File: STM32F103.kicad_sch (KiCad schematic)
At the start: 8 parts, among them SW1 SW_MEC_5E, U1 STM32F103CBTx

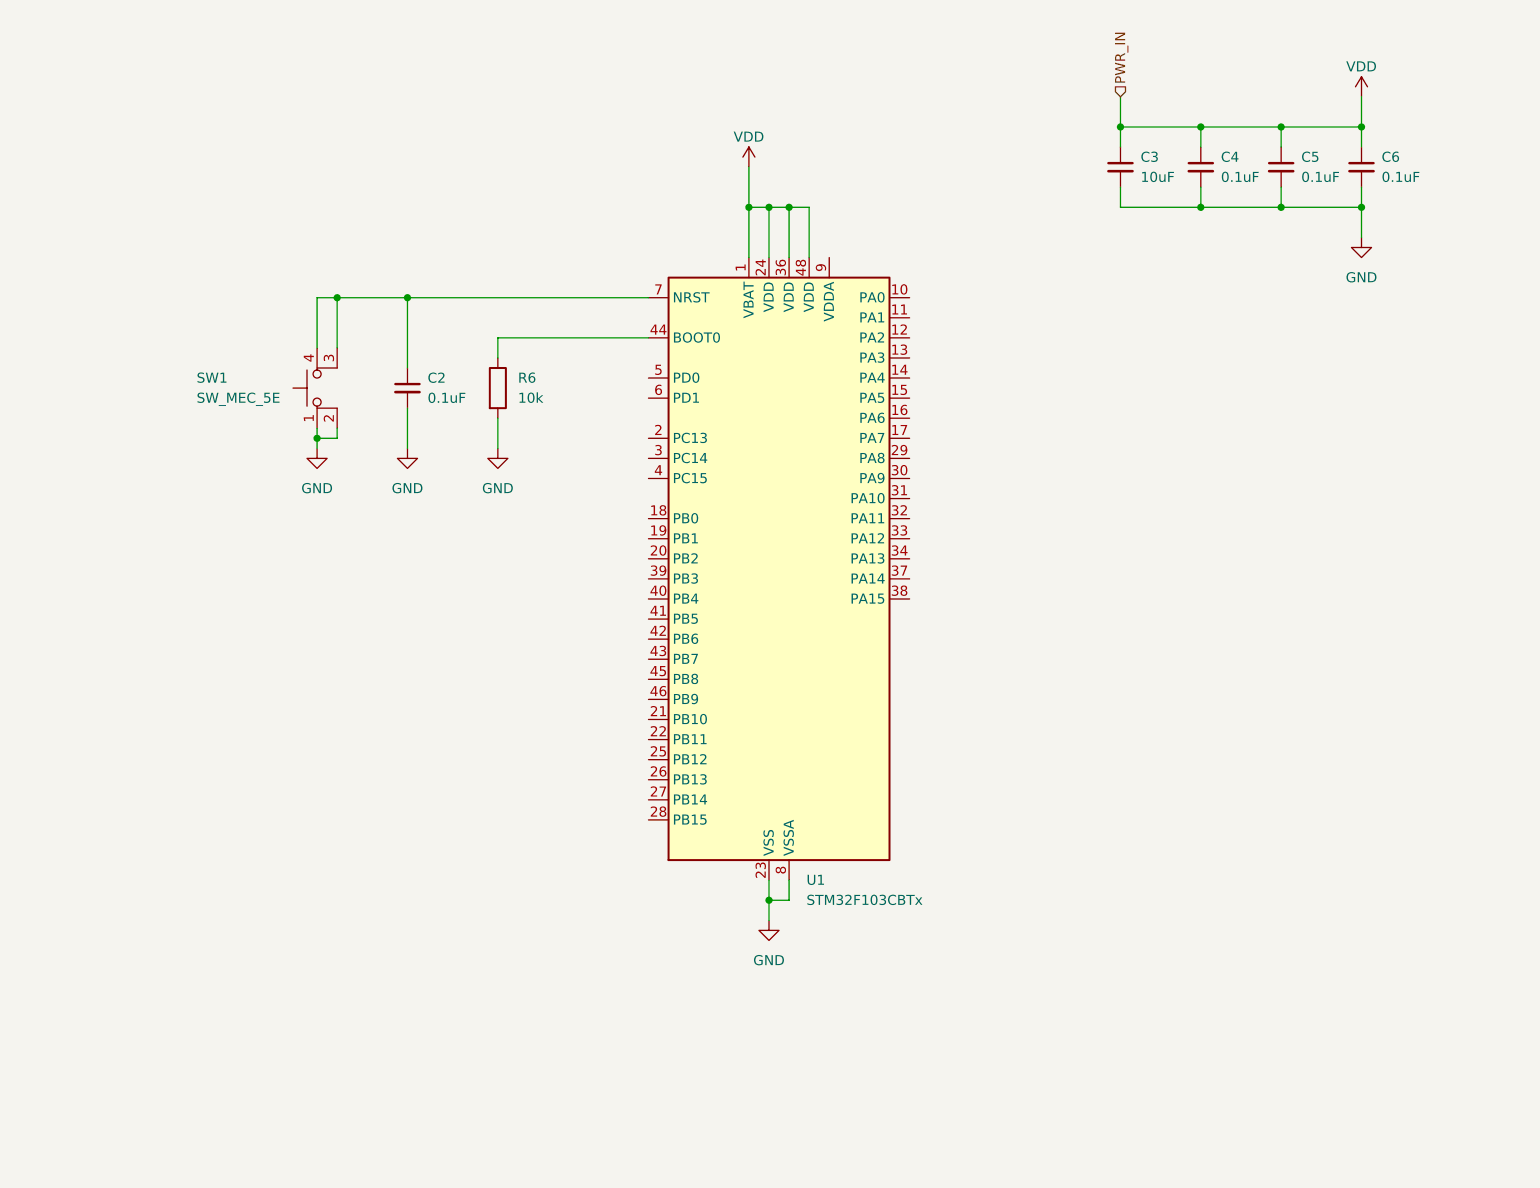
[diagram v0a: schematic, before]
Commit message: add STM32F103
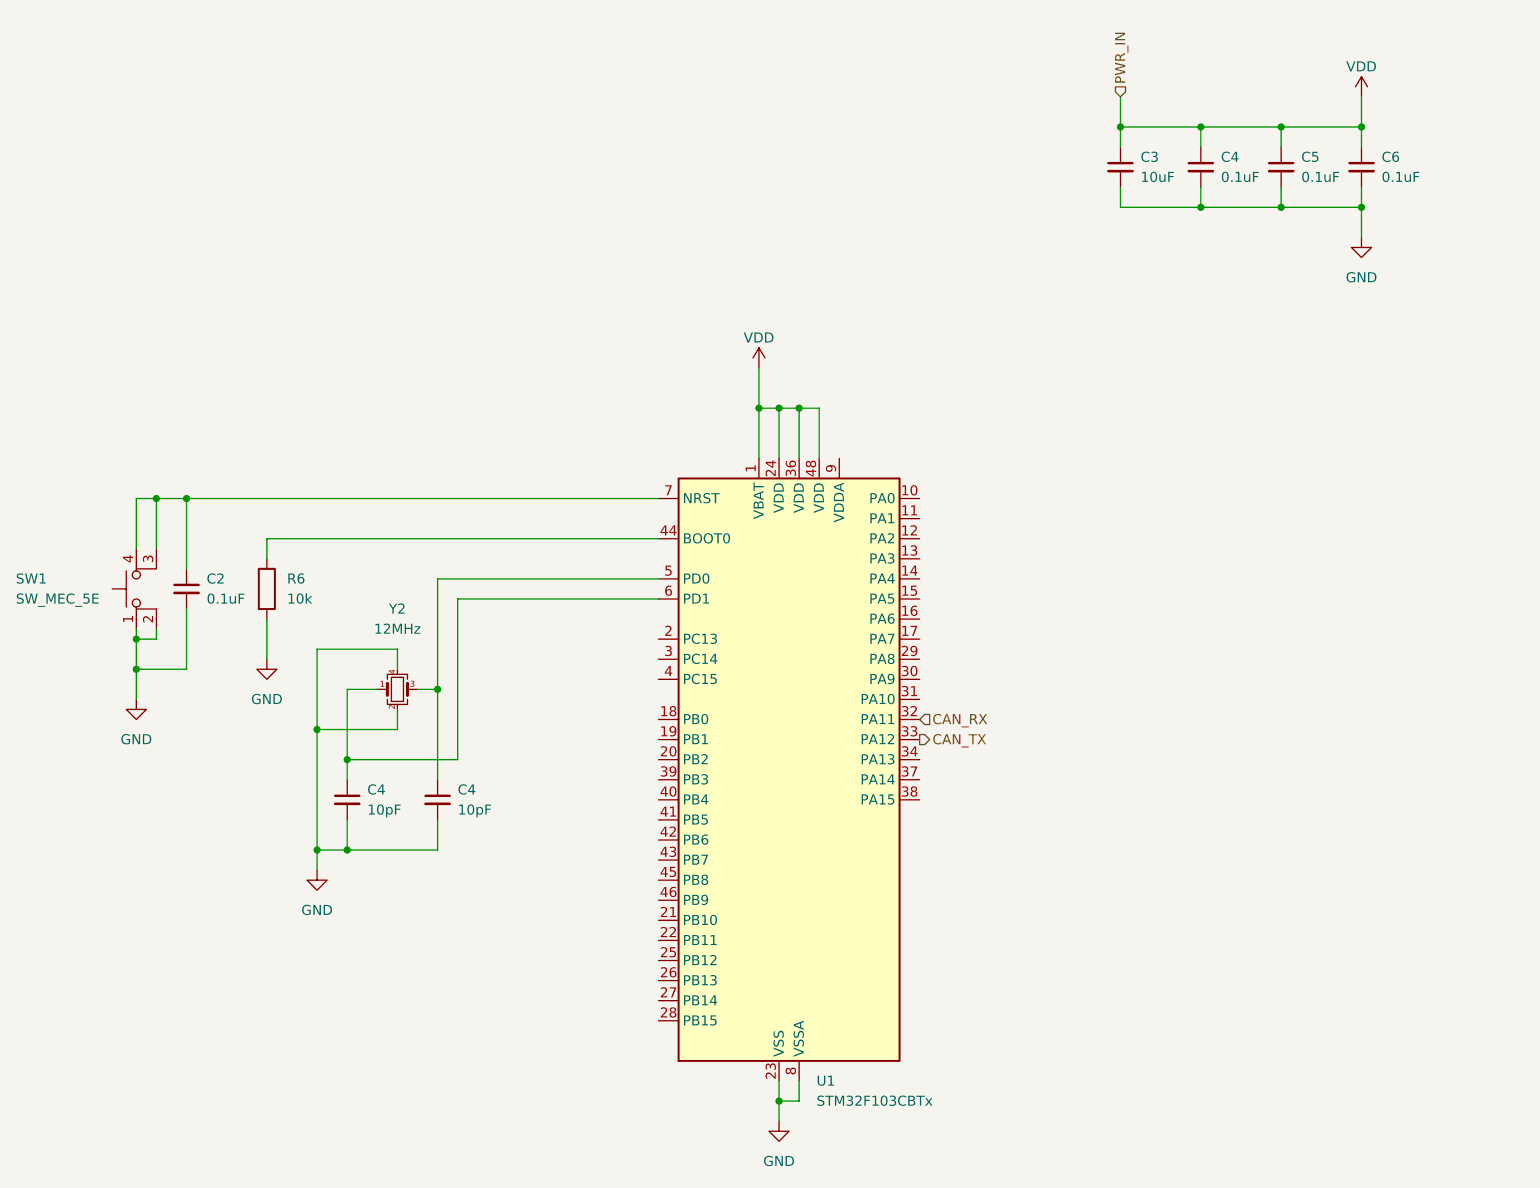
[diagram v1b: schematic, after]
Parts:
- added C4 (x2): 10pF, Capacitor_SMD:C_0603_1608Metric_Pad1.08x0.95mm_HandSolder, symbol Device:C_Small
- added Y2: 12MHz, symbol Device:Crystal_GND24_Small
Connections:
- net GND: now also C4.2, C4.2, Y2.2, Y2.4
- net CAN_RX: now reaches U1.32 (PA11)
- net CAN_TX: now reaches U1.33 (PA12)
- net at U1.5 (PD0): now also C4.1, Y2.3
- net at U1.6 (PD1): now also C4.1, Y2.1
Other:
- moved on the sheet: C2, R6, SW1, U1

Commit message: add switch, EMS & MCU
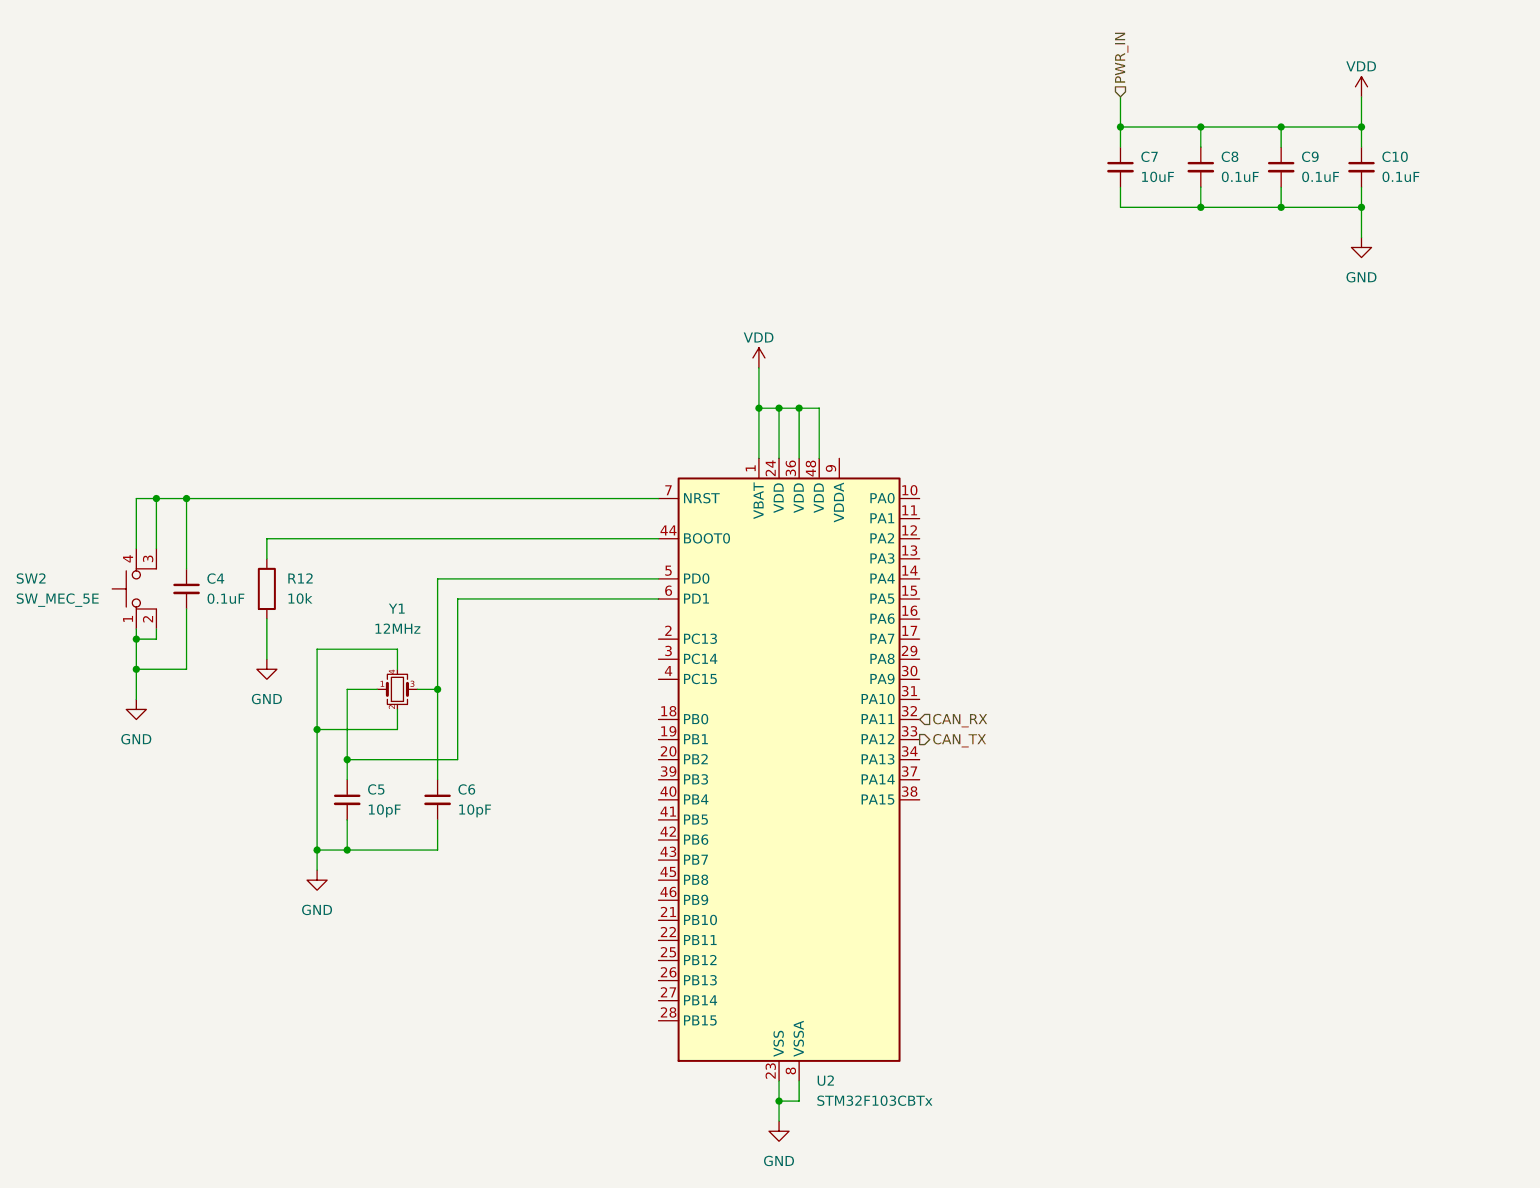
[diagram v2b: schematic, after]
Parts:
- renumbered C6 to C10, C2 to C4, C4 to C5, C4 to C6, C3 to C7, C4 to C8, C5 to C9, R6 to R12, SW1 to SW2, U1 to U2, Y2 to Y1

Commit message: precompreate design
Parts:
- removed SW2: SW_MEC_5E, symbol Switch:SW_MEC_5E
- added C13, C17: 0.1uF, Capacitor_SMD:C_0603_1608Metric_Pad1.08x0.95mm_HandSolder, symbol Device:C_Small
- added C16: 10uF, Capacitor_SMD:C_0603_1608Metric_Pad1.08x0.95mm_HandSolder, symbol Device:C_Small
- added SW4: SW_SPST, Button_Switch_THT:SW_PUSH_6mm_H7.3mm, symbol Switch:SW_SPST
- Y1: footprint (none) -> Crystal:Crystal_SMD_SeikoEpson_FA238V-4Pin_3.2x2.5mm
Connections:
- net GND: now also C13.2, C16.2, C17.2, SW4.1 (A)
- net VDD: now also U2.9 (VDDA), C13.1, C16.1, C17.1
- net CAN_ID1: now reaches U2.13 (PA3)
- net CAN_ID2: now reaches U2.14 (PA4)
- net CAN_ID3: now reaches U2.15 (PA5)
- net CAN_ID4: now reaches U2.16 (PA6)
- net SWDIO: now reaches U2.34 (PA13)
- net SWCLK: now reaches U2.37 (PA14)
- net SWO: now reaches U2.39 (PB3)
- net EMS_Signal: now reaches U2.40 (PB4)
- net EMS_Observe: now reaches U2.41 (PB5)
- net MCU_run: now reaches U2.42 (PB6)
- net at C4.1, U2.7 (NRST): now also SW4.2 (B)
